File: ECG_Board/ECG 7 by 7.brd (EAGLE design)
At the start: 70 x 70 mm, 11 parts

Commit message: Cleanup, organization and updates
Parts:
- removed JP1: (no value), SparkFun-Connectors:1X03
- removed JP3: (no value), SparkFun-Connectors:1X06
- removed STANDOFF1, STANDOFF2, STANDOFF3, STANDOFF4: STAND-OFF, SparkFun-Electromechanical:STAND-OFF
- added FRAME1: FRAME-LETTERNO_PACKAGE, SparkFun-Aesthetics:DUMMY
- added U$1: (no value), SPARK_ECG:SPARK_ECG
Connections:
- net 3.3V: now also U$1.2; no longer JP3.2
- net GND: now also U$1.1; no longer JP3.1
- net N$1: now also U$1.7; no longer JP1.1
- net N$2: now also U$1.8; no longer JP1.2
- net N$3: now also U$1.9; no longer JP1.3
- net N$4: now also U$1.6; no longer JP3.6
- net N$5: now also U$1.5; no longer JP3.5
- net N$6: now also U$1.4; no longer JP3.4
- net N$7: now also U$1.3; no longer JP3.3
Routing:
- net N$3: track 62.5 -> 66.1 mm
- net N$2: track 58.9 -> 61.1 mm
- net N$1: track 55.3 -> 56.6 mm
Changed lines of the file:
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@@
 <wire x1="0" y1="70" x2="0" y2="0" width="0.254" layer="20"/>
 <wire x1="0" y1="0" x2="70" y2="0" width="0.254" layer="20"/>
-<text x="31.59" y="44.828" size="1.27" layer="21" font="vector" ratio="20" rot="R90" align="center-left">GND</text>
-<text x="34.13" y="44.828" size="1.27" layer="21" font="vector" ratio="20" rot="R90" align="center-left">3.3v</text>
-<text x="44.29" y="44.828" size="1.27" layer="21" font="vector" ratio="20" rot="R90" align="center-left">!SDN</text>
-<text x="39.21" y="44.828" size="1.27" layer="21" font="vector" ratio="20" rot="R90" align="center-left">LO-</text>
-<text x="41.75" y="44.828" size="1.27" layer="21" font="vector" ratio="20" rot="R90" align="center-left">LO+</text>
-<text x="31.59" y="44.828" size="1.27" layer="22" font="vector" ratio="20" rot="MR90" align="center-left">GND</text>
-<text x="34.13" y="44.828" size="1.27" layer="22" font="vector" ratio="20" rot="MR90" align="center-left">3.3v</text>
-<text x="39.21" y="44.828" size="1.27" layer="22" font="vector" ratio="20" rot="MR90" align="center-left">LO-</text>
-<text x="41.75" y="44.828" size="1.27" layer="22" font="vector" ratio="20" rot="MR90" align="center-left">LO+</text>
-<text x="44.29" y="44.828" size="1.27" layer="22" font="vector" ratio="20" rot="MR90" align="center-left">!SDN</text>
-<text x="36.67" y="44.701" size="1.27" layer="21" font="vector" ratio="20" rot="R90" align="center-left">OUTPUT</text>
-<text x="36.67" y="44.701" size="1.27" layer="22" font="vector" ratio="20" rot="MR90" align="center-left">OUTPUT</text>
-<text x="23.208" y="59.56" size="1.27" layer="21" font="vector" ratio="15" align="center-left">LA</text>
-<text x="23.208" y="62.1" size="1.27" layer="21" font="vector" ratio="15" align="center-left">RA</text>
-<text x="23.208" y="57.02" size="1.27" layer="21" font="vector" ratio="15" align="center-left">RL</text>
-<dimension x1="0" y1="0" x2="0" y2="70" x3="0" y3="35" textsize="1.778" layer="1"/>
+<dimension x1="-5" y1="0" x2="-5" y2="70" x3="0" y3="35" textsize="1.778" layer="1"/>
 <hole x="4" y="66.25" drill="3.5"/>
 <hole x="66.25" y="66.25" drill="3.5"/>
@@
 <text x="2" y="59" size="1.778" layer="25" rot="R270">ECG Board
 MediBrick2000</text>
-<dimension x1="33.274" y1="67.31" x2="0" y2="67" x3="16.6934" y3="61.101325" textsize="1.778" layer="1"/>
+<dimension x1="30.5" y1="72" x2="0" y2="72" x3="15.25" y3="75" textsize="1.778" layer="1"/>
 </plain>
 <attributes>
@@
 </autorouter>
 <elements>
-<element name="STANDOFF4" library="SparkFun-Electromechanical" package="STAND-OFF" value="STAND-OFF" x="22.7" y="44.32" smashed="yes" rot="R180"/>
-<element name="STANDOFF3" library="SparkFun-Electromechanical" package="STAND-OFF" value="STAND-OFF" x="53.18" y="44.32" smashed="yes"/>
-<element name="STANDOFF1" library="SparkFun-Electromechanical" package="STAND-OFF" value="STAND-OFF" x="22.7" y="67.18" smashed="yes"/>
-<element name="STANDOFF2" library="SparkFun-Electromechanical" package="STAND-OFF" value="STAND-OFF" x="53.18" y="67.18" smashed="yes"/>
-<element name="JP3" library="SparkFun-Connectors" package="1X06" value="" x="31.59" y="43.05" smashed="yes">
-<attribute name="NAME" x="45.2438" y="40.8788" size="1.27" layer="25" ratio="10"/>
-<attribute name="VALUE" x="30.32" y="39.875" size="1.27" layer="27"/>
-</element>
-<element name="JP1" library="SparkFun-Connectors" package="1X03" value="" x="21.43" y="57.02" smashed="yes" rot="R90">
-<attribute name="NAME" x="19.6012" y="55.6738" size="1.27" layer="25" ratio="10" rot="R90"/>
-<attribute name="VALUE" x="24.605" y="55.75" size="1.27" layer="27" rot="R90"/>
-</element>
 <element name="JP2" library="SparkFun-Connectors" package="1X06" value="" x="46" y="5" smashed="yes">
 <attribute name="NAME" x="58.6538" y="2.8288" size="1.27" layer="25" ratio="10"/>
@@
 <attribute name="VALUE" x="26" y="7.143" size="0.6096" layer="27" font="vector" ratio="20" rot="R180" align="top-center"/>
 </element>
+<element name="FRAME1" library="SparkFun-Aesthetics" library_urn="urn:adsk.eagle:library:507" package="DUMMY" package3d_urn="urn:adsk.eagle:package:37104/1" value="FRAME-LETTERNO_PACKAGE" x="-3" y="-1" smashed="yes">
+<attribute name="DESIGNER" value="Nobody" x="-3" y="-1" size="1.778" layer="27" display="off"/>
+<attribute name="VERSION" value="v01" x="-3" y="-1" size="1.778" layer="27" display="off"/>
+</element>
+<element name="U$1" library="SPARK_ECG" package="SPARK_ECG" value="" x="20" y="42" smashed="yes"/>
 </elements>
 <signals>
-<signal name="N$1">
-<contactref element="JP1" pad="1"/>
-<contactref element="JP4" pad="1"/>
-<wire x1="21.43" y1="57.02" x2="16" y2="51.59" width="0.1778" layer="1"/>
-<wire x1="16" y1="51.59" x2="16" y2="4" width="0.1778" layer="1"/>
-</signal>
-<signal name="N$2">
-<contactref element="JP1" pad="2"/>
-<contactref element="JP4" pad="2"/>
-<wire x1="21.43" y1="59.56" x2="13.46" y2="51.59" width="0.1778" layer="1"/>
-<wire x1="13.46" y1="51.59" x2="13.46" y2="4" width="0.1778" layer="1"/>
-</signal>
-<signal name="N$3">
-<contactref element="JP1" pad="3"/>
-<contactref element="JP4" pad="3"/>
-<wire x1="21.43" y1="62.1" x2="10.92" y2="51.59" width="0.1778" layer="1"/>
-<wire x1="10.92" y1="51.59" x2="10.92" y2="4" width="0.1778" layer="1"/>
-</signal>
 <signal name="N$4">
-<contactref element="JP3" pad="6"/>
 <contactref element="JP2" pad="6"/>
-<wire x1="44.29" y1="43.05" x2="44.29" y2="19.41" width="0.4064" layer="1"/>
-<wire x1="44.29" y1="19.41" x2="58.7" y2="5" width="0.4064" layer="1"/>
+<wire x1="44.29" y1="19.41" x2="44.35" y2="19.35" width="0.4064" layer="1"/>
+<contactref element="U$1" pad="6"/>
+<wire x1="44.35" y1="19.35" x2="58.7" y2="5" width="0.4064" layer="1"/>
+<wire x1="44.13" y1="43.27" x2="44.13" y2="19.57" width="0.4064" layer="1"/>
+<wire x1="44.13" y1="19.57" x2="44.29" y2="19.41" width="0.4064" layer="1"/>
 </signal>
 <signal name="N$5">
-<contactref element="JP3" pad="5"/>
 <contactref element="JP2" pad="5"/>
-<wire x1="41.75" y1="43.05" x2="41.75" y2="19.41" width="0.4064" layer="1"/>
-<wire x1="41.75" y1="19.41" x2="56.16" y2="5" width="0.4064" layer="1"/>
+<contactref element="U$1" pad="5"/>
+<wire x1="41.59" y1="19.57" x2="41.59" y2="43.27" width="0.4064" layer="1"/>
+<wire x1="56.16" y1="5" x2="41.59" y2="19.57" width="0.4064" layer="1"/>
 </signal>
 <signal name="N$6">
-<contactref element="JP3" pad="4"/>
 <contactref element="JP2" pad="4"/>
-<wire x1="39.21" y1="43.05" x2="39.21" y2="19.41" width="0.4064" layer="1"/>
-<wire x1="39.21" y1="19.41" x2="53.62" y2="5" width="0.4064" layer="1"/>
+<contactref element="U$1" pad="4"/>
+<wire x1="39.05" y1="19.57" x2="39.05" y2="43.27" width="0.4064" layer="1"/>
+<wire x1="53.62" y1="5" x2="39.05" y2="19.57" width="0.4064" layer="1"/>
 </signal>
 <signal name="N$7">
-<contactref element="JP3" pad="3"/>
 <contactref element="JP2" pad="3"/>
-<wire x1="36.67" y1="43.05" x2="36.67" y2="19.41" width="0.4064" layer="1"/>
-<wire x1="36.67" y1="19.41" x2="51.08" y2="5" width="0.4064" layer="1"/>
+<contactref element="U$1" pad="3"/>
+<wire x1="36.51" y1="43.27" x2="36.51" y2="19.57" width="0.4064" layer="1"/>
+<wire x1="36.51" y1="19.57" x2="51.08" y2="5" width="0.4064" layer="1"/>
 </signal>
 <signal name="3.3V">
-<contactref element="JP3" pad="2"/>
 <contactref element="JP2" pad="2"/>
-<wire x1="34.13" y1="43.05" x2="34.13" y2="19.41" width="0.4064" layer="1"/>
-<wire x1="34.13" y1="19.41" x2="48.54" y2="5" width="0.4064" layer="1"/>
 <contactref element="R16" pad="2"/>
 <wire x1="39.85" y1="3" x2="46.54" y2="3" width="0.4064" layer="1"/>
 <wire x1="46.54" y1="3" x2="48.54" y2="5" width="0.4064" layer="1"/>
+<contactref element="U$1" pad="2"/>
+<wire x1="33.97" y1="43.27" x2="33.97" y2="19.57" width="0.4064" layer="1"/>
+<wire x1="33.97" y1="19.57" x2="48.54" y2="5" width="0.4064" layer="1"/>
 </signal>
 <signal name="N$26">
@@
 <vertex x="0" y="0"/>
 </polygon>
-<contactref element="JP3" pad="1"/>
 <contactref element="JP2" pad="1"/>
-<wire x1="31.59" y1="43.05" x2="31.59" y2="19.41" width="0.4064" layer="1"/>
-<wire x1="31.59" y1="19.41" x2="46" y2="5" width="0.4064" layer="1"/>
+<wire x1="31.59" y1="19.41" x2="32" y2="19" width="0.4064" layer="1"/>
 <contactref element="LED_DISABLE" pad="1"/>
+<wire x1="32" y1="19" x2="46" y2="5" width="0.4064" layer="1"/>
 <wire x1="26.508" y1="5" x2="46" y2="5" width="0.4064" layer="1"/>
 <polygon width="0.1524" layer="16">
@@
 <vertex x="0" y="0"/>
 </polygon>
+<contactref element="U$1" pad="1"/>
+<wire x1="31.43" y1="43.27" x2="31.43" y2="19.57" width="0.4064" layer="1"/>
+<wire x1="31.43" y1="19.57" x2="31.59" y2="19.41" width="0.4064" layer="1"/>
+</signal>
+<signal name="N$1">
+<contactref element="JP4" pad="1"/>
+<contactref element="U$1" pad="7"/>
+<wire x1="21.27" y1="57.24" x2="21.03" y2="57" width="0.4064" layer="1"/>
+<wire x1="21.03" y1="57" x2="19" y2="57" width="0.4064" layer="1"/>
+<wire x1="16" y1="54" x2="16" y2="4" width="0.4064" layer="1"/>
+<wire x1="19" y1="57" x2="16" y2="54" width="0.4064" layer="1"/>
+</signal>
+<signal name="N$2">
+<contactref element="JP4" pad="2"/>
+<contactref element="U$1" pad="8"/>
+<wire x1="13.46" y1="4" x2="13.46" y2="55.46" width="0.4064" layer="1"/>
+<wire x1="17.78" y1="59.78" x2="21.27" y2="59.78" width="0.4064" layer="1"/>
+<wire x1="13.46" y1="55.46" x2="17.78" y2="59.78" width="0.4064" layer="1"/>
+</signal>
+<signal name="N$3">
+<contactref element="JP4" pad="3"/>
+<contactref element="U$1" pad="9"/>
+<wire x1="21.27" y1="62.32" x2="20.95" y2="62" width="0.4064" layer="1"/>
+<wire x1="20.95" y1="62" x2="15" y2="62" width="0.4064" layer="1"/>
+<wire x1="15" y1="62" x2="11" y2="58" width="0.4064" layer="1"/>
+<wire x1="11" y1="4.08" x2="10.92" y2="4" width="0.4064" layer="1"/>
+<wire x1="11" y1="58" x2="11" y2="4.08" width="0.4064" layer="1"/>
 </signal>
 </signals>

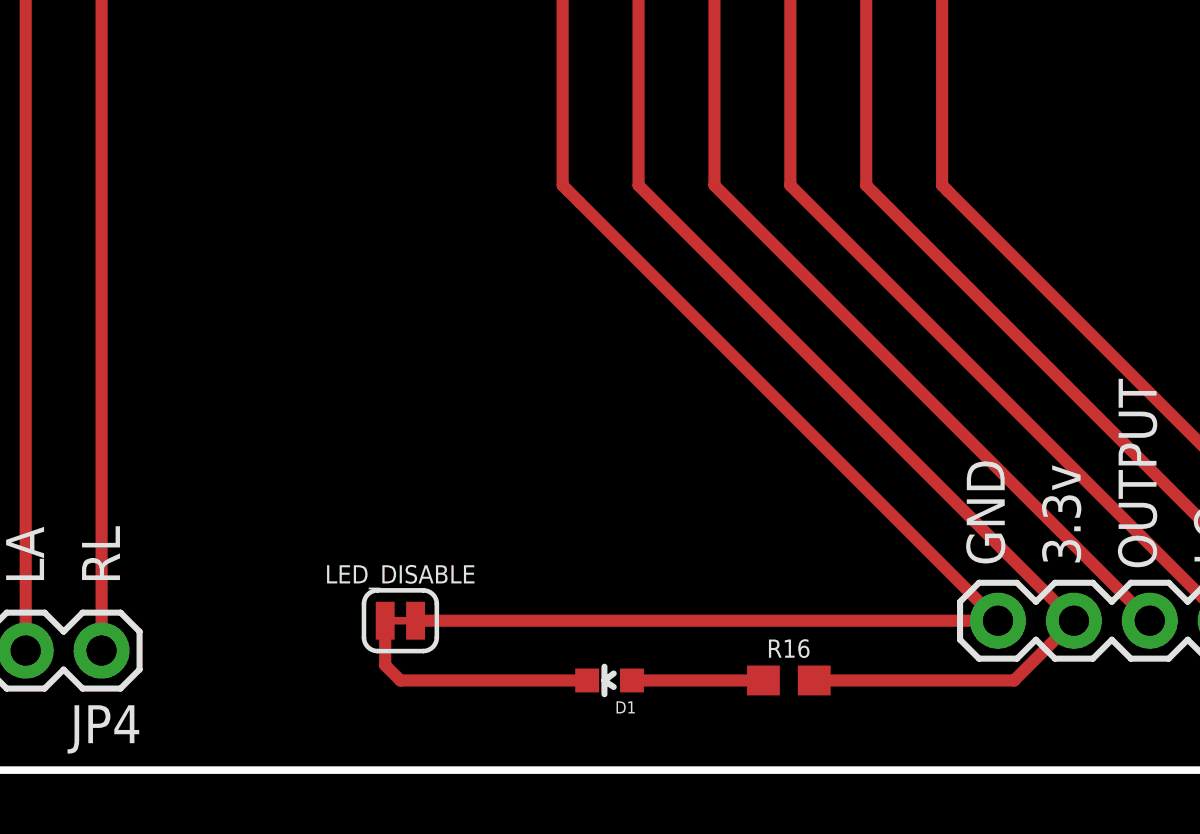
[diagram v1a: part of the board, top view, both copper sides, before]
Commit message: Board Updates
All LEDs at same location
Separated analog and digital ground
Updated impedance components
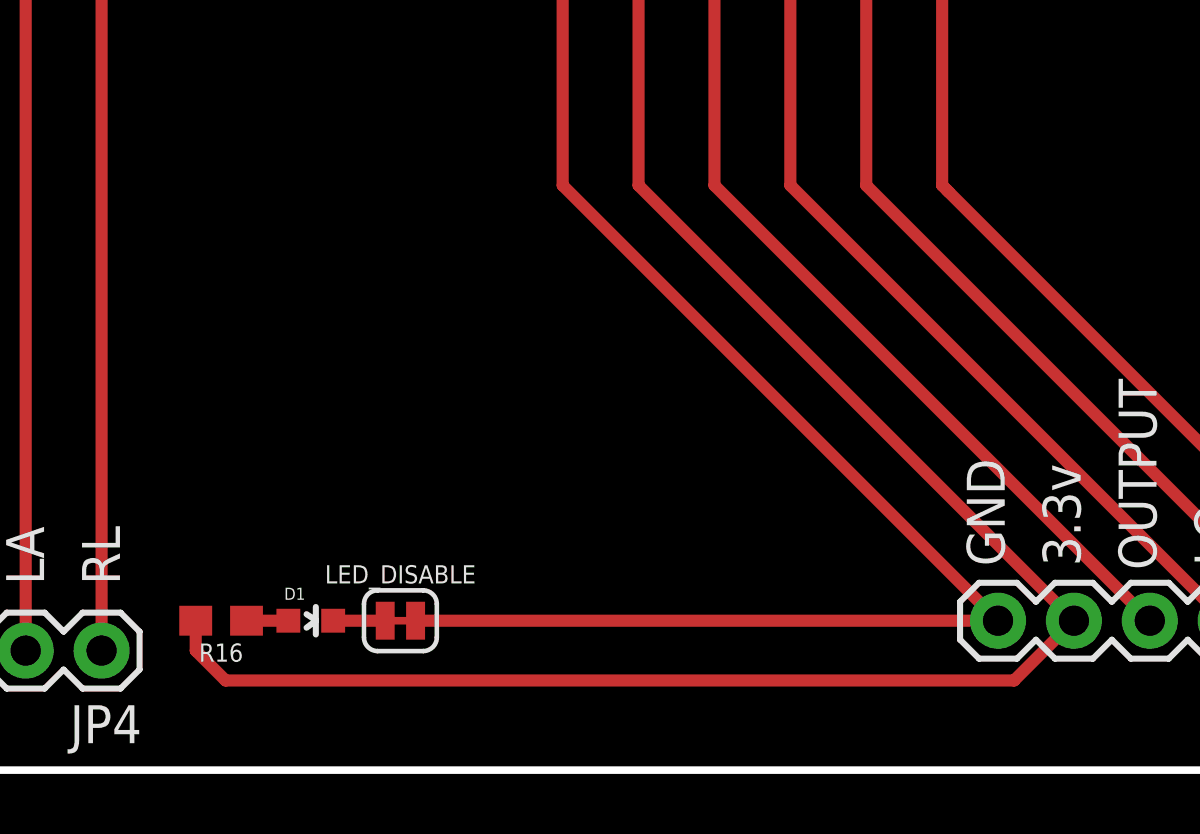
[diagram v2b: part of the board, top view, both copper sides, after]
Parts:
- moved R16 19.1 mm to (20.0, 5.00), turned to 180 degrees
- moved D1 10.2 mm to (23.0, 5.00), turned to 270 degrees
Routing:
- net 3.3V: track 53.8 -> 75.9 mm
- net N$28: track 8.46 -> 1.74 mm
- net N$26: track 4.40 -> 1.40 mm
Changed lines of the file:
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@@
 <drawing>
 <settings>
-<setting alwaysvectorfont="no"/>
+<setting alwaysvectorfont="yes"/>
 <setting keepoldvectorfont="yes"/>
 <setting verticaltext="up"/>
@@
 <attribute name="VALUE" x="17.27" y="7.175" size="1.27" layer="27" rot="R180"/>
 </element>
-<element name="R16" library="SparkFun-Resistors" library_urn="urn:adsk.eagle:library:532" package="0603" package3d_urn="urn:adsk.eagle:package:39650/1" value="1k" x="39" y="3" smashed="yes">
-<attribute name="NAME" x="39" y="3.762" size="0.6096" layer="25" font="vector" ratio="20" align="bottom-center"/>
-<attribute name="PROD_ID" value="RES-07856" x="39" y="8" size="1.778" layer="27" display="off"/>
-<attribute name="VALUE" x="39" y="2.238" size="0.6096" layer="27" font="vector" ratio="20" align="top-center"/>
+<element name="R16" library="SparkFun-Resistors" library_urn="urn:adsk.eagle:library:532" package="0603" package3d_urn="urn:adsk.eagle:package:39650/1" value="1k" x="20" y="5" smashed="yes" rot="R180">
+<attribute name="NAME" x="20" y="4.238" size="0.6096" layer="25" font="vector" ratio="20" rot="R180" align="bottom-center"/>
+<attribute name="PROD_ID" value="RES-07856" x="20" y="0" size="1.778" layer="27" rot="R180" display="off"/>
+<attribute name="VALUE" x="20" y="5.762" size="0.6096" layer="27" font="vector" ratio="20" rot="R180" align="top-center"/>
 </element>
-<element name="D1" library="SparkFun-LED" package="LED-0603" value="RED" x="33" y="3" smashed="yes" rot="R90">
-<attribute name="NAME" x="33.889" y="2.3015" size="0.4064" layer="25" rot="R180"/>
-<attribute name="PROD_ID" value="DIO-00819" x="28" y="-4" size="1.778" layer="27" rot="R90" display="off"/>
-<attribute name="VALUE" x="34.016" y="4.0795" size="0.4064" layer="27" rot="R180"/>
+<element name="D1" library="SparkFun-LED" package="LED-0603" value="RED" x="23" y="5" smashed="yes" rot="R270">
+<attribute name="NAME" x="22.111" y="5.6985" size="0.4064" layer="25"/>
+<attribute name="PROD_ID" value="DIO-00819" x="28" y="12" size="1.778" layer="27" rot="R270" display="off"/>
+<attribute name="VALUE" x="21.984" y="3.9205" size="0.4064" layer="27"/>
 </element>
 <element name="LED_DISABLE" library="SparkFun-Jumpers" library_urn="urn:adsk.eagle:library:528" package="SMT-JUMPER_2_NC_TRACE_SILK" package3d_urn="urn:adsk.eagle:package:39281/1" value="JUMPER-SMT_2_NC_TRACE_SILK" x="26" y="5" smashed="yes" rot="R180">
@@
 <contactref element="JP2" pad="2"/>
 <contactref element="R16" pad="2"/>
-<wire x1="39.85" y1="3" x2="46.54" y2="3" width="0.4064" layer="1"/>
+<wire x1="46.54" y1="3" x2="20.15" y2="3" width="0.4064" layer="1"/>
+<wire x1="20.15" y1="3" x2="19.15" y2="4" width="0.4064" layer="1"/>
+<wire x1="19.15" y1="5" x2="19.15" y2="4" width="0.4064" layer="1"/>
 <wire x1="46.54" y1="3" x2="48.54" y2="5" width="0.4064" layer="1"/>
 <contactref element="U$1" pad="2"/>
@@
 <contactref element="R16" pad="1"/>
 <contactref element="D1" pad="A"/>
-<wire x1="33.75" y1="3" x2="38.15" y2="3" width="0.4064" layer="1"/>
+<wire x1="22.25" y1="5" x2="20.85" y2="5" width="0.4064" layer="1"/>
 </signal>
 <signal name="N$28">
 <contactref element="D1" pad="C"/>
 <contactref element="LED_DISABLE" pad="2"/>
-<wire x1="25.492" y1="5" x2="25.492" y2="3.508" width="0.4064" layer="1"/>
-<wire x1="25.492" y1="3.508" x2="26" y2="3" width="0.4064" layer="1"/>
-<wire x1="26" y1="3" x2="32.25" y2="3" width="0.4064" layer="1"/>
+<wire x1="23.75" y1="5" x2="25.492" y2="5" width="0.4064" layer="1"/>
 </signal>
 <signal name="GND">
-<polygon width="0.1524" layer="1">
+<polygon width="0.1524" layer="1" isolate="0.254">
 <vertex x="0" y="70"/>
 <vertex x="70" y="70"/>
@@
 </polygon>
 <contactref element="JP2" pad="1"/>
-<wire x1="31.59" y1="19.41" x2="32" y2="19" width="0.4064" layer="1"/>
 <contactref element="LED_DISABLE" pad="1"/>
-<wire x1="32" y1="19" x2="46" y2="5" width="0.4064" layer="1"/>
-<wire x1="26.508" y1="5" x2="46" y2="5" width="0.4064" layer="1"/>
-<polygon width="0.1524" layer="16">
+<wire x1="31.43" y1="19.57" x2="46" y2="5" width="0.4064" layer="1"/>
+<wire x1="46" y1="5" x2="26.508" y2="5" width="0.4064" layer="1"/>
+<polygon width="0.1524" layer="16" isolate="0.254">
 <vertex x="0" y="70"/>
 <vertex x="70" y="70"/>
@@
 <contactref element="U$1" pad="1"/>
 <wire x1="31.43" y1="43.27" x2="31.43" y2="19.57" width="0.4064" layer="1"/>
-<wire x1="31.43" y1="19.57" x2="31.59" y2="19.41" width="0.4064" layer="1"/>
 </signal>
 <signal name="N$1">
